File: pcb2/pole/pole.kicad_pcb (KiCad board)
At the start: 2 copper layers, 15 x 39 mm, 25 parts, among them IC1 LMx93, IC2 STM32F0xxKxUx, P1 POWER_IN, P2 BUS_IN, P3 BUS_OUT, P4 SWD_TC, P5 LEDs, Q1 MTM232270LBF, Q2 MTM232270LBF, Q3 MTM232270LBF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

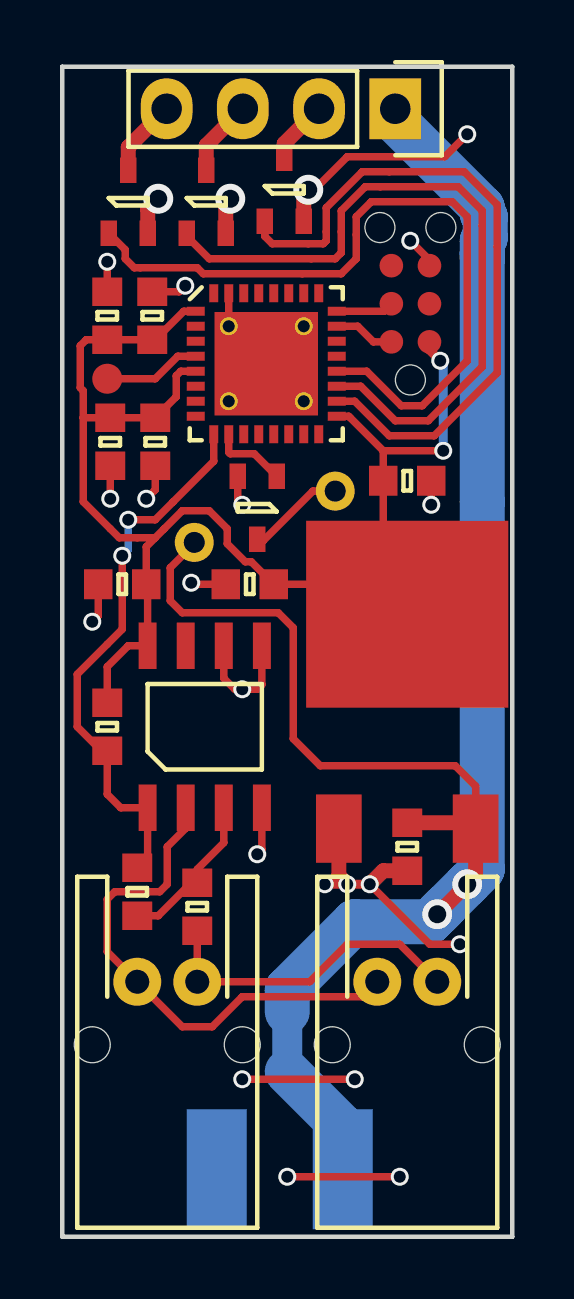
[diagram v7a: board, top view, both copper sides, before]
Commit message: Changed vias from 0.6/0.4 to 0.6/0.3
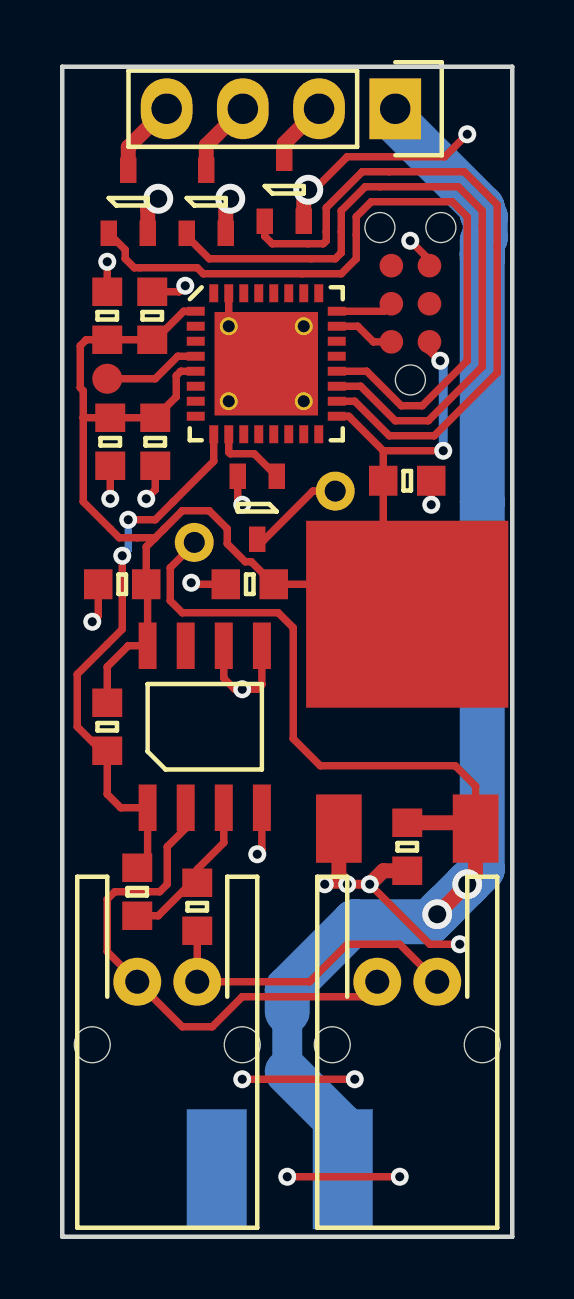
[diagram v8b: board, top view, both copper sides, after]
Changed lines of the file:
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@@
   (gr_line (start 116 76) (end 131 76) (angle 90) (layer Edge.Cuts) (width 0.15))
   (gr_line (start 131 115) (end 116 115) (angle 90) (layer Edge.Cuts) (width 0.15))
-  (via (at 122 109.75) (size 0.6) (drill 0.4) (layers F.Cu B.Cu) (net 0))
-  (via (at 125.75 109.75) (size 0.6) (drill 0.4) (layers F.Cu B.Cu) (net 0))
+  (via (at 122 109.75) (size 0.6) (drill 0.3) (layers F.Cu B.Cu) (net 0))
+  (via (at 125.75 109.75) (size 0.6) (drill 0.3) (layers F.Cu B.Cu) (net 0))
   (segment (start 122 109.75) (end 125.75 109.75) (width 0.25) (layer F.Cu) (net 0))
-  (via (at 123.5 113) (size 0.6) (drill 0.4) (layers F.Cu B.Cu) (net 0))
-  (via (at 127.25 113) (size 0.6) (drill 0.4) (layers F.Cu B.Cu) (net 0))
+  (via (at 123.5 113) (size 0.6) (drill 0.3) (layers F.Cu B.Cu) (net 0))
+  (via (at 127.25 113) (size 0.6) (drill 0.3) (layers F.Cu B.Cu) (net 0))
   (segment (start 123.5 113) (end 127.25 113) (width 0.25) (layer F.Cu) (net 0))
   (segment (start 124.2 80.1) (end 124.4 80.1) (width 0.25) (layer F.Cu) (net 1))
@@
   (via (at 124.2 80.1) (size 1) (drill 0.6) (layers F.Cu B.Cu) (net 1))
   (segment (start 124.05 81.15) (end 124.05 80.25) (width 0.5) (layer F.Cu) (net 1))
-  (via (at 129.5 78.25) (size 0.6) (drill 0.4) (layers F.Cu B.Cu) (net 1))
+  (via (at 129.5 78.25) (size 0.6) (drill 0.3) (layers F.Cu B.Cu) (net 1))
   (segment (start 128.75 79) (end 129.5 78.25) (width 0.25) (layer F.Cu) (net 1))
   (segment (start 125.5 79) (end 128.75 79) (width 0.25) (layer F.Cu) (net 1))
   (segment (start 124.4 80.1) (end 125.5 79) (width 0.25) (layer F.Cu) (net 1))
   (segment (start 126.25 103.25) (end 128.25 105.25) (width 0.25) (layer F.Cu) (net 1))
-  (via (at 126.25 103.25) (size 0.6) (drill 0.4) (layers F.Cu B.Cu) (net 1))
-  (via (at 129.25 105.25) (size 0.6) (drill 0.4) (layers F.Cu B.Cu) (net 1))
+  (via (at 126.25 103.25) (size 0.6) (drill 0.3) (layers F.Cu B.Cu) (net 1))
+  (via (at 129.25 105.25) (size 0.6) (drill 0.3) (layers F.Cu B.Cu) (net 1))
   (segment (start 128.25 105.25) (end 129.25 105.25) (width 0.25) (layer F.Cu) (net 1))
   (segment (start 121.55 83.55) (end 121.55 84.65) (width 0.25) (layer F.Cu) (net 1))
   (segment (start 127.5 102.8) (end 126.7 102.8) (width 0.5) (layer F.Cu) (net 1))
   (segment (start 126.25 103.25) (end 125.5 103.25) (width 0.3) (layer F.Cu) (net 1))
-  (via (at 125.5 103.25) (size 0.6) (drill 0.4) (layers F.Cu B.Cu) (net 1))
+  (via (at 125.5 103.25) (size 0.6) (drill 0.3) (layers F.Cu B.Cu) (net 1))
   (segment (start 126.7 102.8) (end 126.25 103.25) (width 0.5) (layer F.Cu) (net 1))
   (segment (start 121.45 81.55) (end 121.45 80.55) (width 0.5) (layer F.Cu) (net 1))
@@
   (segment (start 118.85 80.75) (end 119.2 80.4) (width 0.5) (layer F.Cu) (net 1))
   (segment (start 119 83.5) (end 119.9 83.5) (width 0.25) (layer F.Cu) (net 1))
-  (via (at 120.1 83.3) (size 0.6) (drill 0.4) (layers F.Cu B.Cu) (net 1))
+  (via (at 120.1 83.3) (size 0.6) (drill 0.3) (layers F.Cu B.Cu) (net 1))
   (segment (start 119.9 83.5) (end 120.1 83.3) (width 0.25) (layer F.Cu) (net 1))
   (segment (start 128.24 82.63) (end 128.24 82.44) (width 0.25) (layer F.Cu) (net 1))
   (segment (start 128.24 82.44) (end 127.6 81.8) (width 0.25) (layer F.Cu) (net 1))
-  (via (at 127.6 81.8) (size 0.6) (drill 0.4) (layers F.Cu B.Cu) (net 1))
+  (via (at 127.6 81.8) (size 0.6) (drill 0.3) (layers F.Cu B.Cu) (net 1))
   (segment (start 128.3 89.8) (end 128.3 90.6) (width 0.25) (layer F.Cu) (net 1))
-  (via (at 128.3 90.6) (size 0.6) (drill 0.4) (layers F.Cu B.Cu) (net 1))
+  (via (at 128.3 90.6) (size 0.6) (drill 0.3) (layers F.Cu B.Cu) (net 1))
   (segment (start 119.1 89.3) (end 119.1 90.1) (width 0.25) (layer F.Cu) (net 1))
-  (via (at 118.8 90.4) (size 0.6) (drill 0.4) (layers F.Cu B.Cu) (net 1))
+  (via (at 118.8 90.4) (size 0.6) (drill 0.3) (layers F.Cu B.Cu) (net 1))
   (segment (start 119.1 90.1) (end 118.8 90.4) (width 0.25) (layer F.Cu) (net 1))
   (segment (start 121.85 89.65) (end 121.85 90.45) (width 0.25) (layer F.Cu) (net 1))
-  (via (at 122 90.6) (size 0.6) (drill 0.4) (layers F.Cu B.Cu) (net 1))
+  (via (at 122 90.6) (size 0.6) (drill 0.3) (layers F.Cu B.Cu) (net 1))
   (segment (start 121.85 90.45) (end 122 90.6) (width 0.25) (layer F.Cu) (net 1))
   (segment (start 117.5 83.5) (end 117.5 82.5) (width 0.25) (layer F.Cu) (net 1))
-  (via (at 117.5 82.5) (size 0.6) (drill 0.4) (layers F.Cu B.Cu) (net 1))
+  (via (at 117.5 82.5) (size 0.6) (drill 0.3) (layers F.Cu B.Cu) (net 1))
   (segment (start 117.6 89.3) (end 117.6 90.4) (width 0.25) (layer F.Cu) (net 1))
-  (via (at 117.6 90.4) (size 0.6) (drill 0.4) (layers F.Cu B.Cu) (net 1))
+  (via (at 117.6 90.4) (size 0.6) (drill 0.3) (layers F.Cu B.Cu) (net 1))
   (segment (start 121.45 93.25) (end 120.35 93.25) (width 0.25) (layer F.Cu) (net 1))
-  (via (at 120.3 93.2) (size 0.6) (drill 0.4) (layers F.Cu B.Cu) (net 1))
+  (via (at 120.3 93.2) (size 0.6) (drill 0.3) (layers F.Cu B.Cu) (net 1))
   (segment (start 120.35 93.25) (end 120.3 93.2) (width 0.25) (layer F.Cu) (net 1))
   (segment (start 117.2 93.25) (end 117.2 94.3) (width 0.25) (layer F.Cu) (net 1))
-  (via (at 117 94.5) (size 0.6) (drill 0.4) (layers F.Cu B.Cu) (net 1))
+  (via (at 117 94.5) (size 0.6) (drill 0.3) (layers F.Cu B.Cu) (net 1))
   (segment (start 117.2 94.3) (end 117 94.5) (width 0.25) (layer F.Cu) (net 1))
   (segment (start 121.385 94.885) (end 121.385 95.3) (width 0.25) (layer F.Cu) (net 1))
@@
   (segment (start 125.22 102.97) (end 125.5 103.25) (width 0.5) (layer F.Cu) (net 1))
   (segment (start 124.75 103.25) (end 125.5 103.25) (width 0.3) (layer F.Cu) (net 1))
-  (via (at 124.75 103.25) (size 0.6) (drill 0.4) (layers F.Cu B.Cu) (net 1))
+  (via (at 124.75 103.25) (size 0.6) (drill 0.3) (layers F.Cu B.Cu) (net 1))
   (segment (start 122.655 95.3) (end 122.655 96.595) (width 0.25) (layer F.Cu) (net 1))
   (segment (start 121.385 96.385) (end 121.75 96.75) (width 0.25) (layer F.Cu) (net 1))
   (segment (start 121.75 96.75) (end 122 96.75) (width 0.25) (layer F.Cu) (net 1))
-  (via (at 122 96.75) (size 0.6) (drill 0.4) (layers F.Cu B.Cu) (net 1))
+  (via (at 122 96.75) (size 0.6) (drill 0.3) (layers F.Cu B.Cu) (net 1))
   (segment (start 121.385 96.385) (end 121.385 95.3) (width 0.25) (layer F.Cu) (net 1))
   (segment (start 122.5 96.75) (end 122 96.75) (width 0.25) (layer F.Cu) (net 1))
   (segment (start 122.655 96.595) (end 122.5 96.75) (width 0.25) (layer F.Cu) (net 1))
   (segment (start 122.655 100.7) (end 122.655 102.095) (width 0.25) (layer F.Cu) (net 1))
-  (via (at 122.5 102.25) (size 0.6) (drill 0.4) (layers F.Cu B.Cu) (net 1))
+  (via (at 122.5 102.25) (size 0.6) (drill 0.3) (layers F.Cu B.Cu) (net 1))
   (segment (start 122.655 102.095) (end 122.5 102.25) (width 0.25) (layer F.Cu) (net 1))
   (segment (start 128.7 88.8) (end 128.7 85.9) (width 0.3) (layer B.Cu) (net 2))
   (segment (start 126.7 88.8) (end 128.7 88.8) (width 0.25) (layer F.Cu) (net 2))
-  (via (at 128.7 88.8) (size 0.6) (drill 0.4) (layers F.Cu B.Cu) (net 2))
+  (via (at 128.7 88.8) (size 0.6) (drill 0.3) (layers F.Cu B.Cu) (net 2))
   (segment (start 128.6 85.8) (end 128.24 85.44) (width 0.3) (layer F.Cu) (net 2))
-  (via (at 128.6 85.8) (size 0.6) (drill 0.4) (layers F.Cu B.Cu) (net 2))
+  (via (at 128.6 85.8) (size 0.6) (drill 0.3) (layers F.Cu B.Cu) (net 2))
   (segment (start 128.7 85.9) (end 128.6 85.8) (width 0.3) (layer B.Cu) (net 2))
   (segment (start 128.24 85.44) (end 128.24 85.17) (width 0.3) (layer F.Cu) (net 2))
@@
   (segment (start 118.2 91.1) (end 119.1 91.1) (width 0.25) (layer F.Cu) (net 4))
   (segment (start 118.2 92.1) (end 118.2 91.1) (width 0.25) (layer B.Cu) (net 4))
-  (via (at 118.2 91.1) (size 0.6) (drill 0.4) (layers F.Cu B.Cu) (net 4))
+  (via (at 118.2 91.1) (size 0.6) (drill 0.3) (layers F.Cu B.Cu) (net 4))
   (segment (start 118 92.3) (end 118 92.5) (width 0.25) (layer F.Cu) (net 4))
   (segment (start 118 94.75) (end 118 92.5) (width 0.25) (layer F.Cu) (net 4))
@@
   (segment (start 116.5 98) (end 116.5 96.25) (width 0.25) (layer F.Cu) (net 4))
   (segment (start 117.5 95.25) (end 118 94.75) (width 0.25) (layer F.Cu) (net 4))
-  (via (at 118 92.3) (size 0.6) (drill 0.4) (layers F.Cu B.Cu) (net 4))
+  (via (at 118 92.3) (size 0.6) (drill 0.3) (layers F.Cu B.Cu) (net 4))
   (segment (start 118 92.3) (end 118.2 92.1) (width 0.25) (layer B.Cu) (net 4))
   (segment (start 119.1 91.1) (end 119.7 90.5) (width 0.25) (layer F.Cu) (net 4))
